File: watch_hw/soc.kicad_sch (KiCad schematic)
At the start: 21 parts, among them J3 Conn_ARM_SWD_TagConnect_TC203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, U1 STM32WB55CGUx, X1 NX2016SA-32M, X2 NX2012_32K768

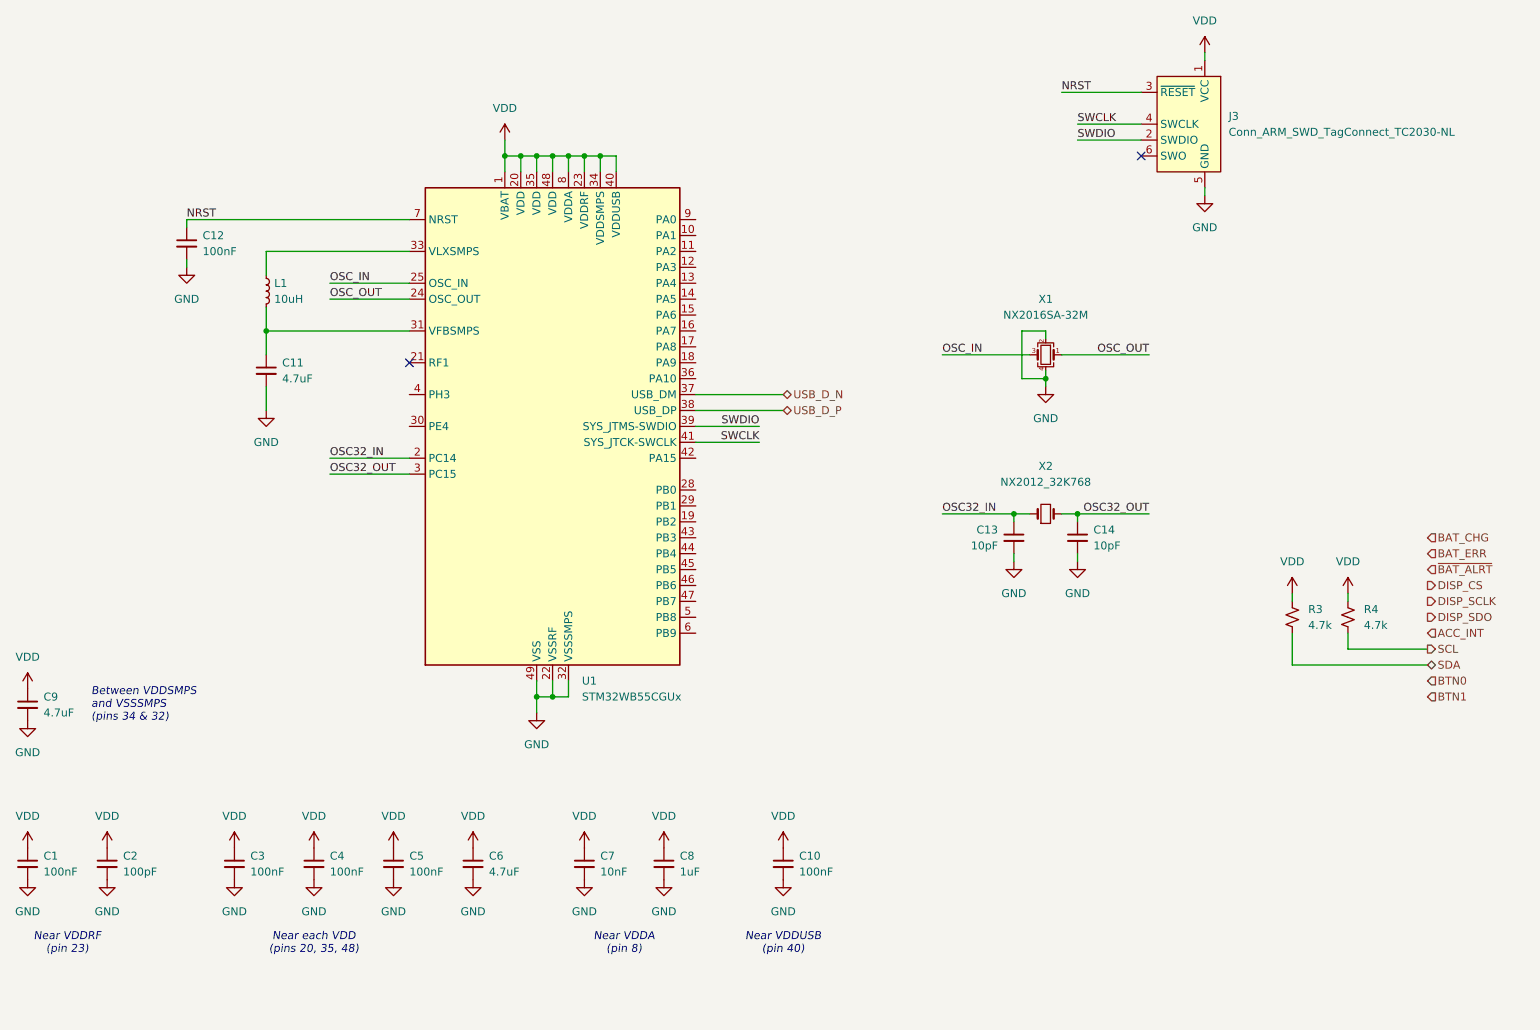
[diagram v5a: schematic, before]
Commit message: route a bunch, update USB plug board edge
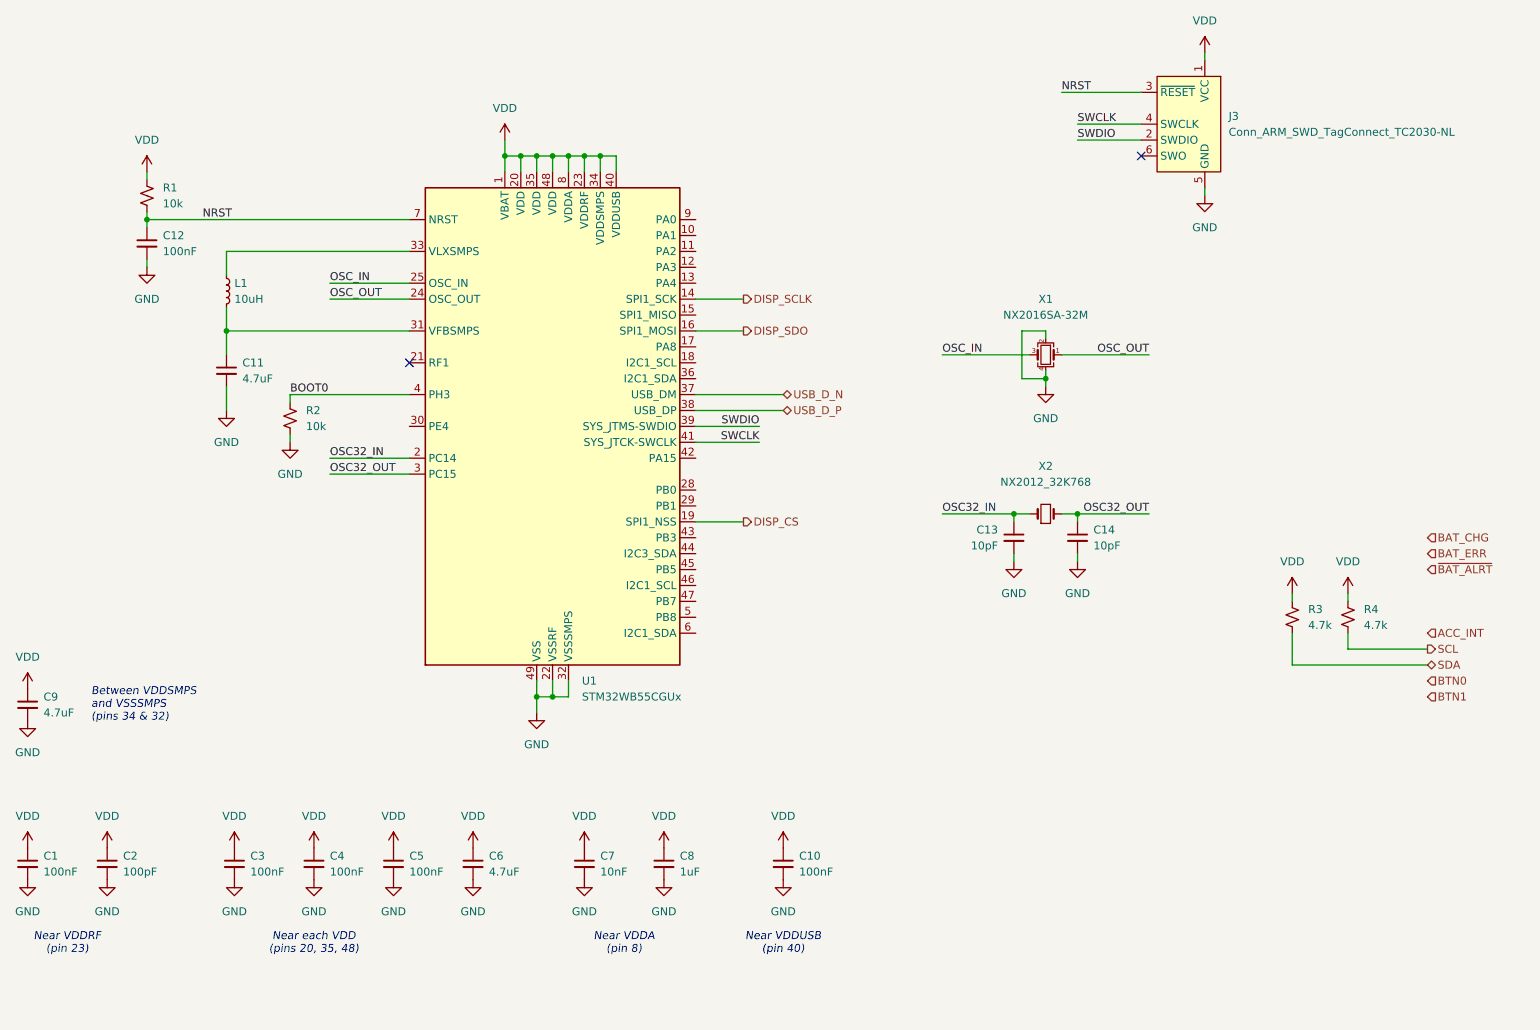
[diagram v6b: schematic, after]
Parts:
- added R1, R2: 10k, Resistor_SMD:R_0402_1005Metric_Pad0.72x0.64mm_HandSolder, symbol Device:R_Small_US
- C11, C9: footprint Capacitor_SMD:C_0402_1005Metric_Pad0.74x0.62mm_HandSolder -> Capacitor_SMD:C_0603_1608Metric_Pad1.08x0.95mm_HandSolder
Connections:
- net DISP_CS: now also U1.19 (PB2)
- net DISP_SCLK: now also U1.14 (PA5)
- net DISP_SDO: now also U1.16 (PA7)
- net GND: now also R2.2
- net NRST: now also R1.2
- net VDD: now also R1.1
- net BOOT0: now reaches U1.4 (PH3)
- net BOOT0: now also R2.1
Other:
- moved on the sheet: C11, C12, L1

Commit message: finish routing, need to fix DRC
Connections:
- net ACC_INT: now also U1.45 (PB5)
- net BAT_CHG: now also U1.43 (PB3)
- net BAT_ERR: now also U1.42 (PA15)
- net BTN0: now also U1.11 (PA2)
- net BTN1: now also U1.12 (PA3)
- net SCL: now also U1.46 (PB6)
- net SDA: now also U1.47 (PB7)
- net ~{BAT_ALRT}: now also U1.44 (PB4)
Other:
- moved on the sheet: C13, C14, R3, R4, X1, X2

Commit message: pass DRC
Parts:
- L1: footprint Inductor_SMD:L_0805_2012Metric_Pad1.15x1.40mm_HandSolder -> Inductor_SMD:L_0805_2012Metric_Pad1.05x1.20mm_HandSolder
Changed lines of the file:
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@@
 			)
 		)
-		(property "Footprint" "Inductor_SMD:L_0805_2012Metric_Pad1.15x1.40mm_HandSolder"
+		(property "Footprint" "Inductor_SMD:L_0805_2012Metric_Pad1.05x1.20mm_HandSolder"
 			(at 69.85 67.31 0)
 			(effects
